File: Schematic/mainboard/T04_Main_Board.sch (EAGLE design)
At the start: 25 parts, among them IC1 7805DT, J1 AVR_SPI_PRG_6PTH, U1 ATMEGA328P_PDIP, X1 22-23-2021, X3 22-23-2081, Y1 16MHZ

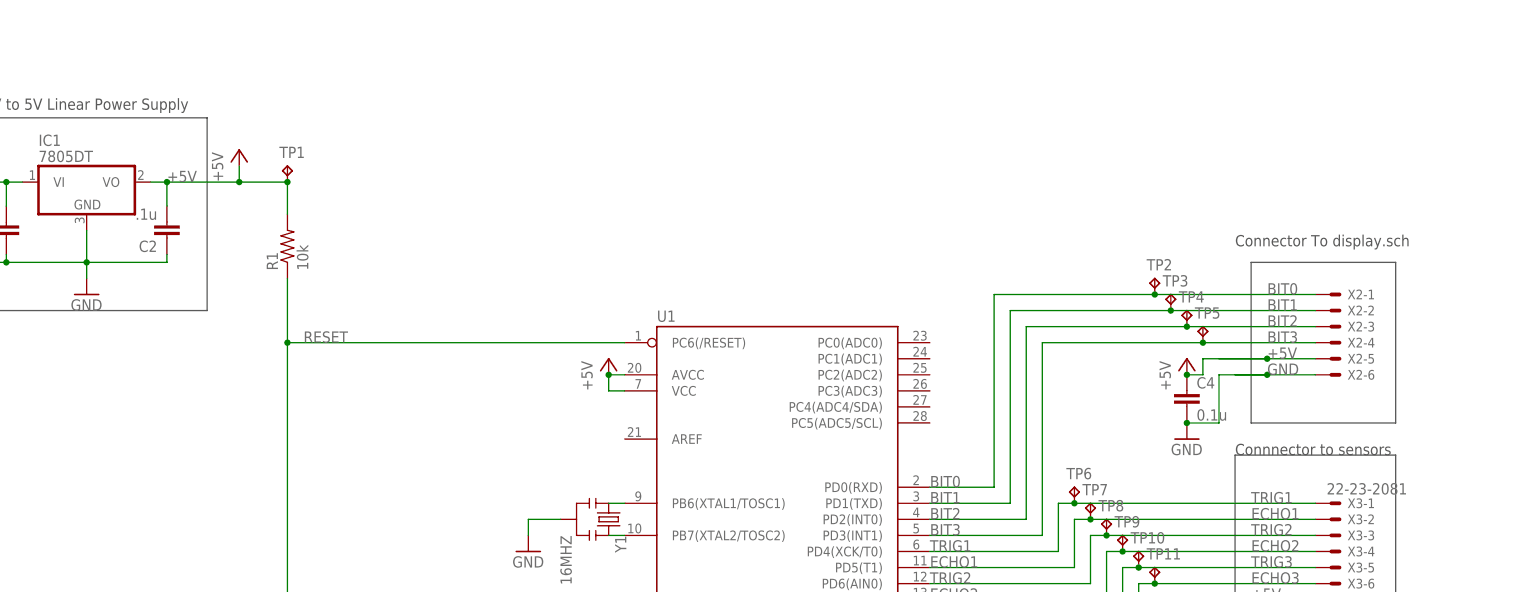
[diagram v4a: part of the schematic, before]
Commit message: Mainboard & Display layout updates - Molex connectors, Mounting Holes, Greenberg Email Additions
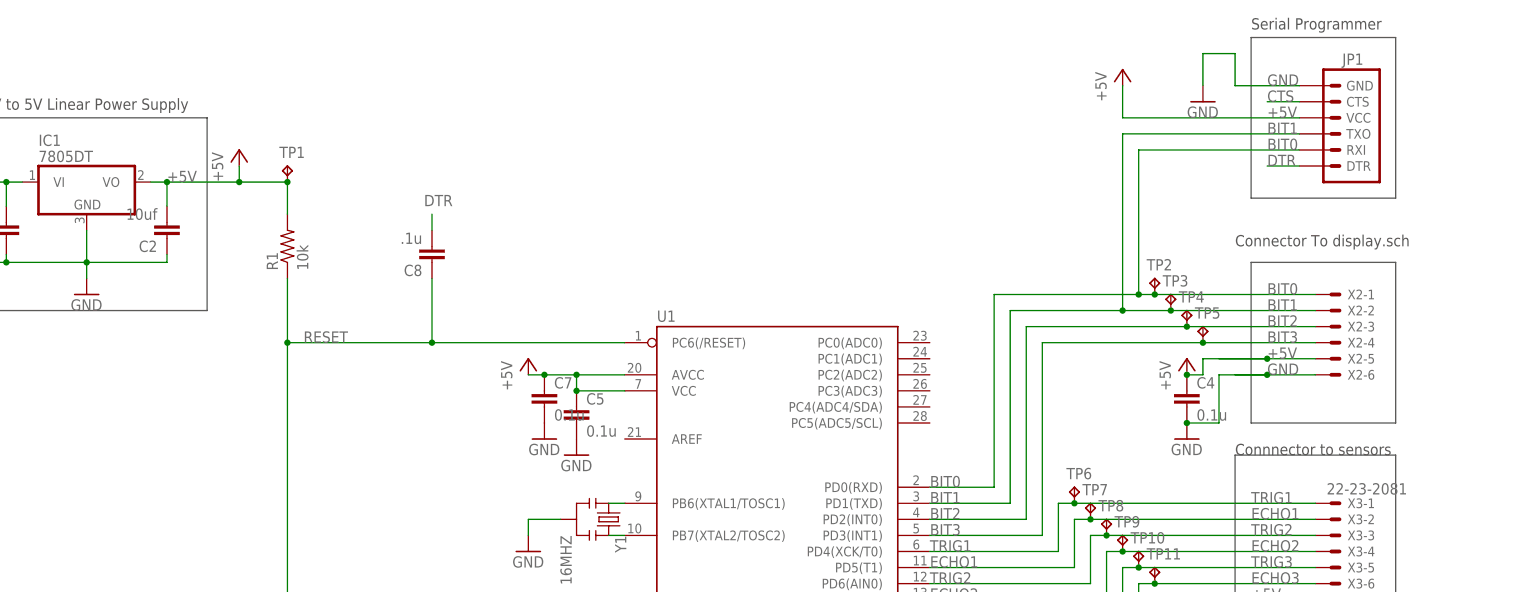
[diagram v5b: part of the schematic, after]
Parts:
- added C5, C7: 0.1u, rcl:C-EU025-024X044
- added C8: .1u, rcl:C-EU025-024X044
- added JP1: (no value), SparkFun-Connectors:ARDUINO_SERIAL_PROGRAMSMD
- C2: value .1u -> 10uf
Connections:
- new net CTS: JP1.CTS
- new net DTR: C8.2, JP1.DTR
- net +5V: now also C5.1, C7.1, JP1.VCC
- net BIT0: now also JP1.RXI
- net BIT1: now also JP1.TXO
- net GND: now also C5.2, C7.2, JP1.GND
- net RESET: now also C8.1
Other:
- note added: "Serial Programmer"

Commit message: M@INb0@RD C0MPl37e
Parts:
- X2: value (none) -> 22-23-2071; device con-molex:22-23-2061 -> con-molex:22-23-2071
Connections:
- new net MUXENABLE: U1.PB2(SS/OC1B), X2-5.S
- net +5V: now also X2-6.S; no longer X2-5.S
- net GND: now also X2-7.S; no longer X2-6.S
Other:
- moved on the sheet: C4
